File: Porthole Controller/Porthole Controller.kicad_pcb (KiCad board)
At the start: 2 copper layers, 65 x 65 mm, 19 parts, among them J1 STRIP1, J2 STRIP2, J3 STRIP3, J4 STRIP4, J5 INMP441, J6 Conn_02x04_Top_Bottom, J7 - +, J8 Conn_01x04, U1 113991054, U2 SN74AHCT125DR

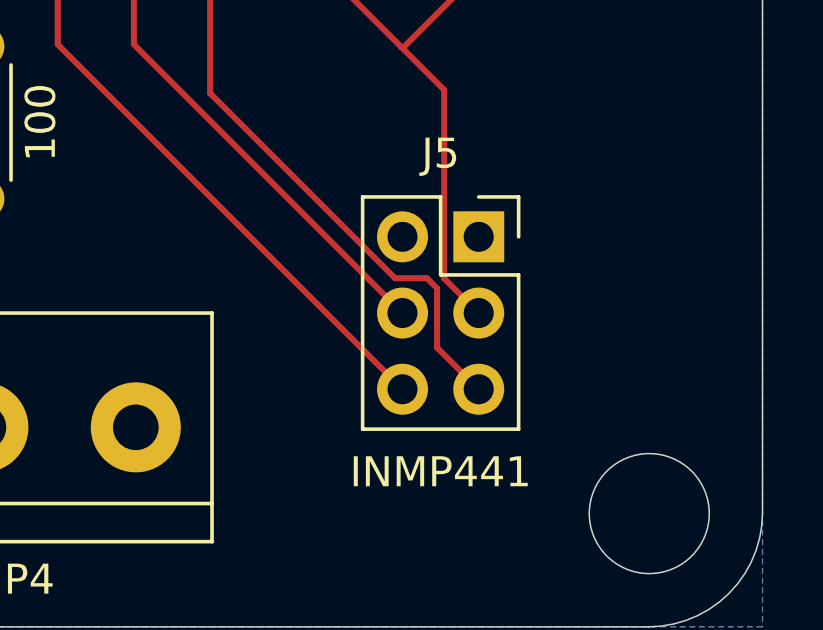
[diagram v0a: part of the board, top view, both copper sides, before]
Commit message: Added silkscreen for INMP441 pinout
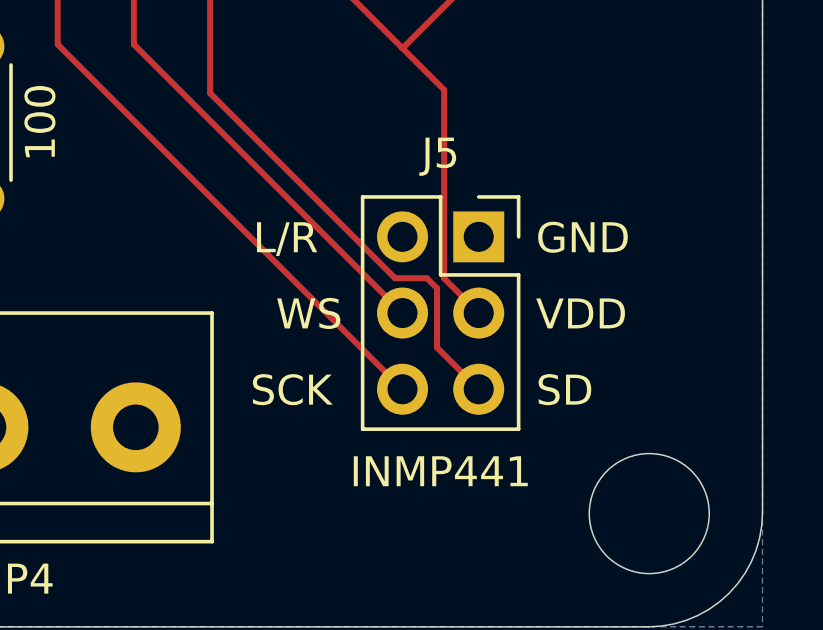
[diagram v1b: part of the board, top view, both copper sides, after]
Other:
- board text added: "L/R"
- board text added: "SCK"
- board text added: "SD"
- board text added: "VDD"
- board text added: "WS"
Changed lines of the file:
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@@
+		)
+	)
+	(gr_text "SCK"
+		(at 185.42 132.715 0)
+		(layer "F.SilkS")
+		(effects
+			(font
+				(size 1 1)
+				(thickness 0.1)
+			)
+			(justify left bottom)
 		)
 	)
@@
 		)
 	)
+	(gr_text "VDD"
+		(at 194.945 130.175 0)
+		(layer "F.SilkS")
+		(effects
+			(font
+				(size 1 1)
+				(thickness 0.1)
+			)
+			(justify left bottom)
+		)
+	)
+	(gr_text "SD"
+		(at 194.945 132.715 0)
+		(layer "F.SilkS")
+		(effects
+			(font
+				(size 1 1)
+				(thickness 0.1)
+			)
+			(justify left bottom)
+		)
+	)
 	(gr_text "D5"
 		(at 185.674 98.425 0)
@@
 		(layer "F.SilkS")
 		(effects
+			(font
+				(size 1 1)
+				(thickness 0.1)
+			)
+			(justify left bottom)
+		)
+	)
+	(gr_text "WS"
+		(at 186.277143 130.175 0)
+		(layer "F.SilkS")
+		(effects
+			(font
+				(size 1 1)
+				(thickness 0.1)
+			)
+			(justify left bottom)
+		)
+	)
+	(gr_text "L/R"
+		(at 185.515238 127.635 0)
+		(layer "F.SilkS")
+		(effects
+			(font
+				(size 1 1)
+				(thickness 0.1)
+			)
+			(justify left bottom)
+		)
+	)
+	(gr_text "GND"
+		(at 194.945 127.635 0)
+		(layer "F.SilkS")
+		(effects

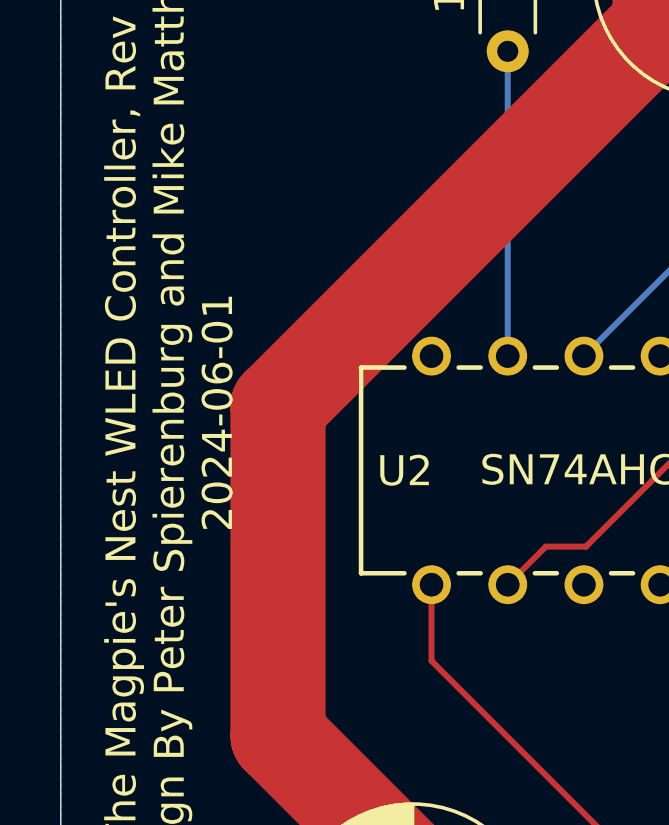
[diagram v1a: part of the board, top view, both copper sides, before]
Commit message: Added variables to silkscreen for revision number and date
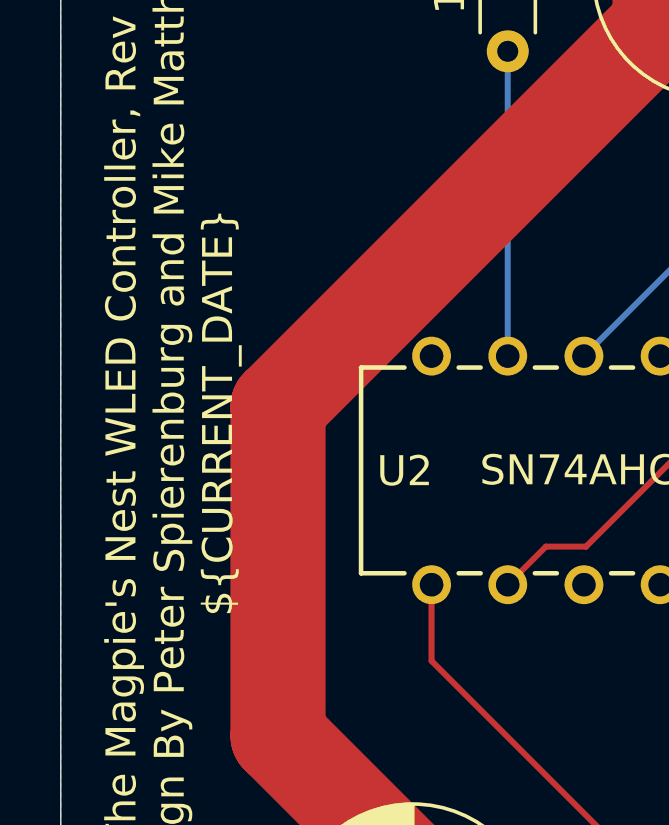
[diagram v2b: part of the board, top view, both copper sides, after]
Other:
- board text added: "The Magpie's Nest WLED Controller, Rev ${REVISION} Design By Peter Spierenburg and Mike Matthews ${CURRENT_DATE}"
- board text removed: "The Magpie's Nest WLED Controller, Rev 1 Design By Peter Spierenburg and Mike Matthews 2024-06-01"
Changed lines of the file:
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@@
 		)
 	)
-	(gr_text "The Magpie's Nest WLED Controller, Rev 1\nDesign By Peter Spierenburg and Mike Matthews\n2024-06-01"
+	(gr_text "The Magpie's Nest WLED Controller, Rev ${REVISION}\nDesign By Peter Spierenburg and Mike Matthews\n${CURRENT_DATE}"
 		(at 143.3322 106.0196 90)
 		(layer "F.SilkS")
